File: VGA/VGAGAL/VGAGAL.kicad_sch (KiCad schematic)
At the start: 27 parts, among them Q2 2N3904, U1 74HCT573, U10 74LVC10, U11 74LVC11, U12 SN74LVC86, U17 74LVC139, U19 74LVC00, U2 74ALVC04, U26 Z80C15CPU_QFP, U27 SST39SF010A-45-4I-NHE, U28 AS7C512, X2 4 MHz

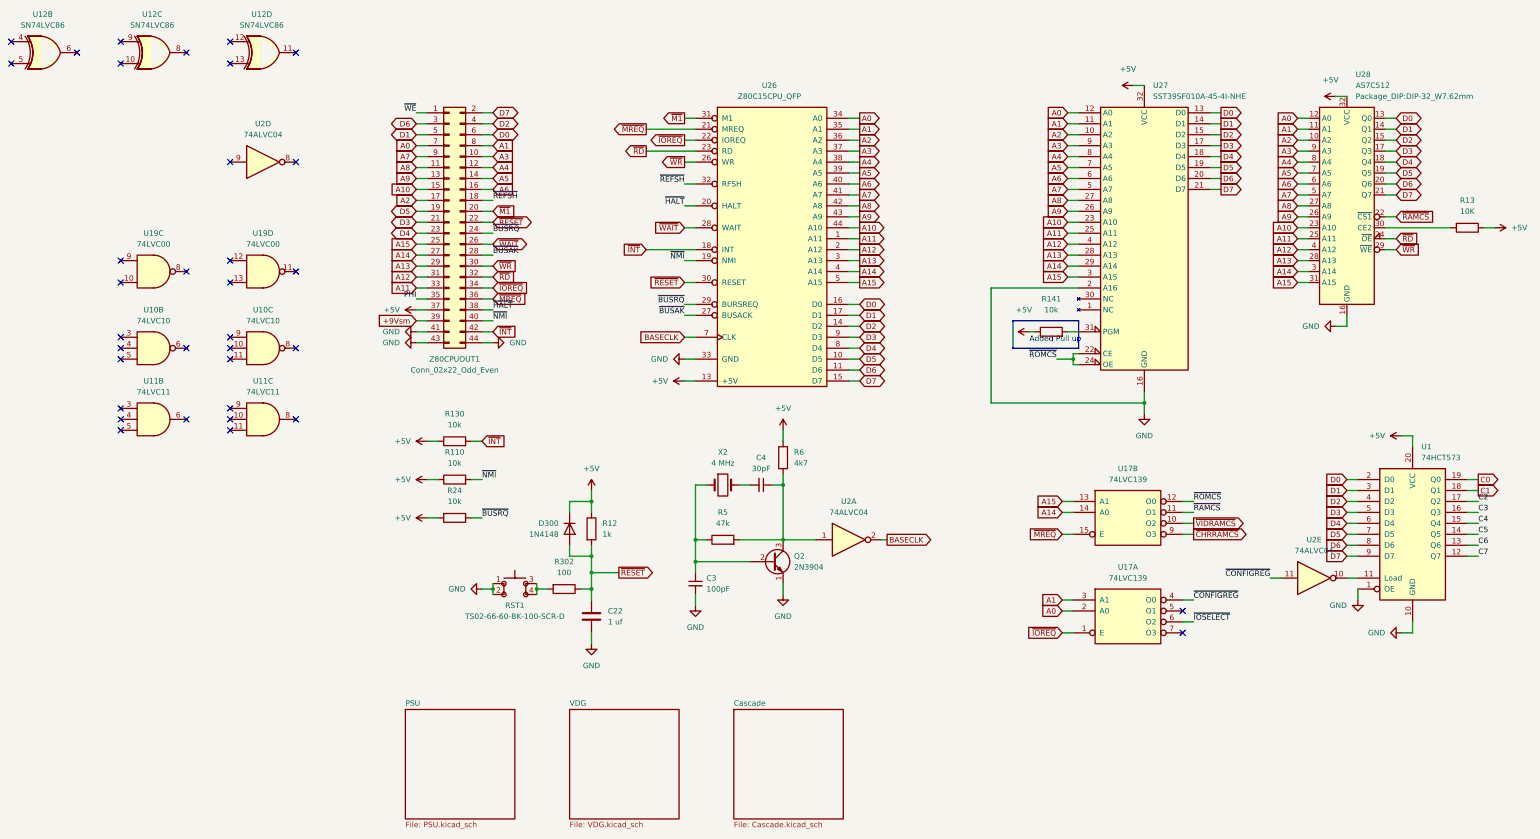
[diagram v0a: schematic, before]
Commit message: Some ideas on VGA.
Signed-off-by: John Bradley <flypie@rocketmail.com>
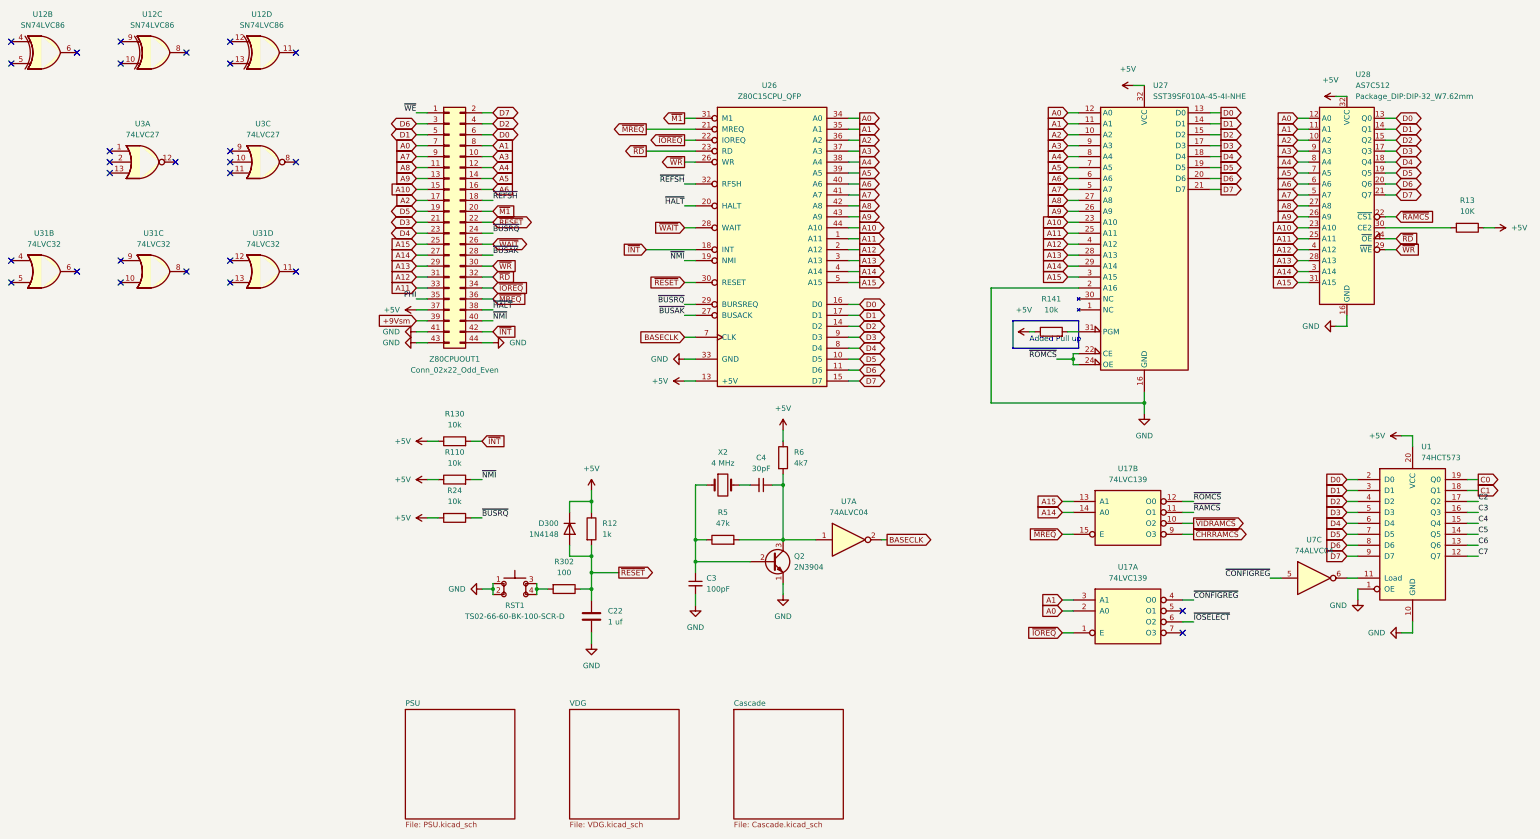
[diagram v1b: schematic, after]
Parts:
- removed U10: 74LVC10, Package_SO:SOIC-14_3.9x8.7mm_P1.27mm, symbol 74xx-FIX:74LS10
- removed U11: 74LVC11, Package_SO:SOIC-14_3.9x8.7mm_P1.27mm, symbol 74xx:74LS11
- removed U19: 74LVC00, Package_SO:SOIC-14_3.9x8.7mm_P1.27mm, symbol 74xx:74LS00
- removed unit 4 of U2
- added U3: 74LVC27, Package_SO:SOIC-14_3.9x8.7mm_P1.27mm, symbol 74xx-FIX:74LS27
- added U31: 74LVC32, Package_SO:SOIC-14_3.9x8.7mm_P1.27mm, symbol 74xx-FIX:74LS32
- renumbered U2 to U7
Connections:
- net ~{CONFIGREG}: now also U7.5; no longer U7.11
- net at U1.11 (Load): now also U7.6; no longer U7.10
- no-connect marks 35 -> 28

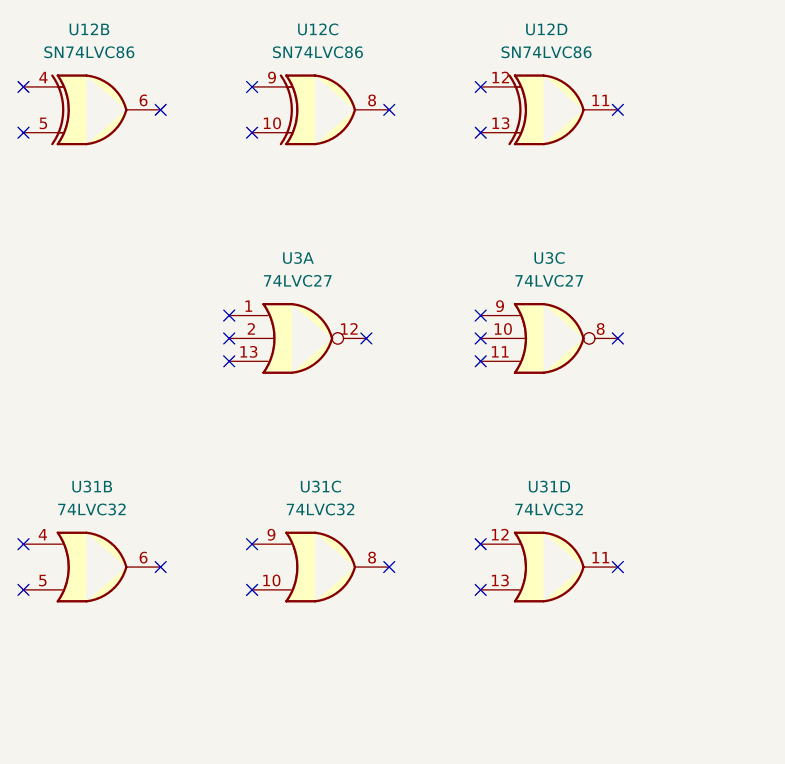
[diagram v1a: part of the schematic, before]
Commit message: Complete Move to KiCAD V6.
Plus various bits of ROM Dev and backups.

Signed-off-by: John Bradley <flypie@rocketmail.com>
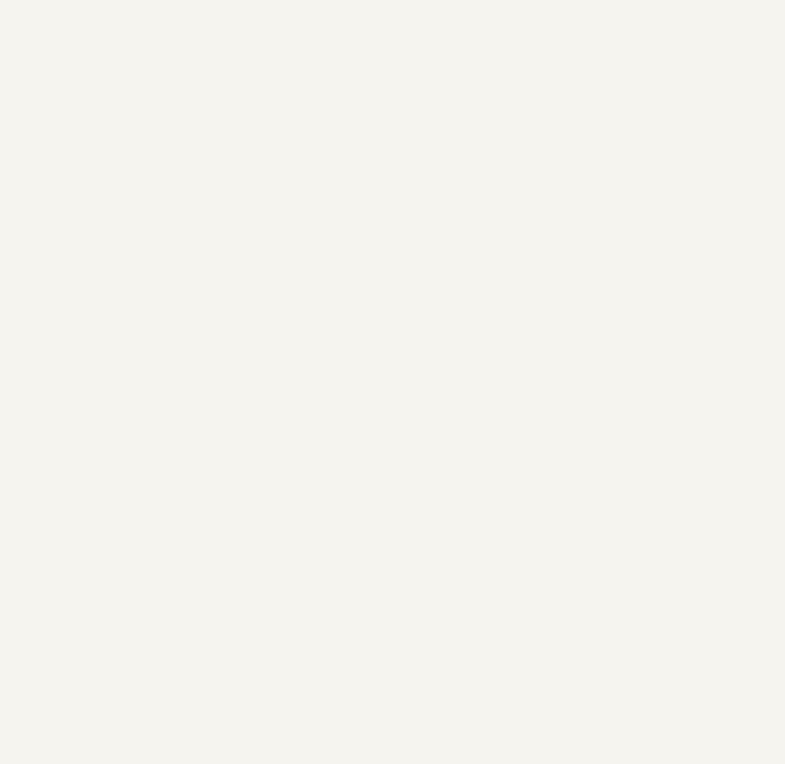
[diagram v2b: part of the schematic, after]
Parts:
- removed U12: SN74LVC86, Package_SO:SOIC-14_3.9x8.7mm_P1.27mm, symbol 74xx:74LS86
- removed U3: 74LVC27, Package_SO:SOIC-14_3.9x8.7mm_P1.27mm, symbol 74xx-FIX:74LS27
- removed U31: 74LVC32, Package_SO:SOIC-14_3.9x8.7mm_P1.27mm, symbol 74xx-FIX:74LS32
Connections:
- no-connect marks 28 -> 2
